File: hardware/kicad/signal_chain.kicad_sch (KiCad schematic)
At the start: 33 parts, among them U901 AD8421ARZ, U902 OPA197IDBV, U903 OPA365AIDBV, U904 ADS8860IDGS

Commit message: feat(hardware)!: draw draft A1 of the schematic around a Pico 2
A Raspberry Pi Pico 2 on two 1x20 sockets replaces the ESP32-S3
development board, the programmable logic device and the buffer
between the two boards (D-39 to D-43 of the specification). The former
interface and range logic sheets become two new ones:

- Controller: the Pico 2, the diodes that join its USB supply and the
  5 V rail of the carrier, resistor arrays in the SPI and acquisition
  lines, a reset button and a console header.
- Side Data: two shift registers that take the range, the status
  signals and the eight logic inputs with every sample.

The DUT connects through a 1x4 pin header and a lever terminal block
in parallel, both GND, VIN, VOUT, GND, and the logic port is a 1x10
header with VCC, GND, D7 to D0: the pin order of the PPK2 (D-44). A
solder jumper selects the supply of the DUT side of the level
translator. A transistor at the driver of the ampere switch holds it
open while VIN is above 5.5 V.

Reference designators are numbered as the annotation tool of KiCad
does by default (D-45). The numbering touches every sheet, so these
changes come in one commit. The symbol and the socket footprint of
the ESP32-S3 board leave the project library; the Pico 2 uses the
symbol and the footprint of the KiCad library.

The electrical rules check reports no errors and no warnings. The
parts stay candidates, and no program for the PIO blocks exists yet.

BREAKING CHANGE: the pins of the controller follow the new pin map of
section 5 of the specification.
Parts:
- renumbered C905 to C57, C908 to C58, C907 to C59, C906 to C60, C901 to C61, C903 to C62, C902 to C63, C909 to C64, C904 to C65, C913 to C66, C912 to C67, C911 to C68, C910 to C69, C914 to C70, C915 to C71, C916 to C72, C917 to C73, C918 to C74, D901 to D10, R902 to R53, R903 to R54, R901 to R55, R904 to R56, R905 to R57, R906 to R58, RN901 to RN3, TP903 to TP22, TP901 to TP23, TP902 to TP24, U902 to U19, U901 to U20, U903 to U21, U904 to U22
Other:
- note added: "U20: G = 1 + 9.9 k / R55 = 19.93. Reference pin at 50 mV: zero current reads about 1300 codes. AMP_RAW can reach 10 V during a range change: R56 and D10 limit the driver input. U21: Sallen-Key, 40 kHz, Q = 0.74. R58 and C70 as the converter input needs. U22: 3-wire mode, DIN high. CONVST is the I2S word clock, SCLK the bit clock. C71 and C72 sit at the REF pin."
- note removed: "U901: G = 1 + 9.9 k / R901 = 19.93. Reference pin at 50 mV: zero current reads about 1300 codes. AMP_RAW can reach 10 V during a range change: R904 and D901 limit the driver input. U903: Sallen-Key, 40 kHz, Q = 0.74. R906 and C914 as the converter input needs. U904: 3-wire mode, DIN high. CONVST is the I2S word clock, SCLK the bit clock. C915 and C916 sit at the REF pin."

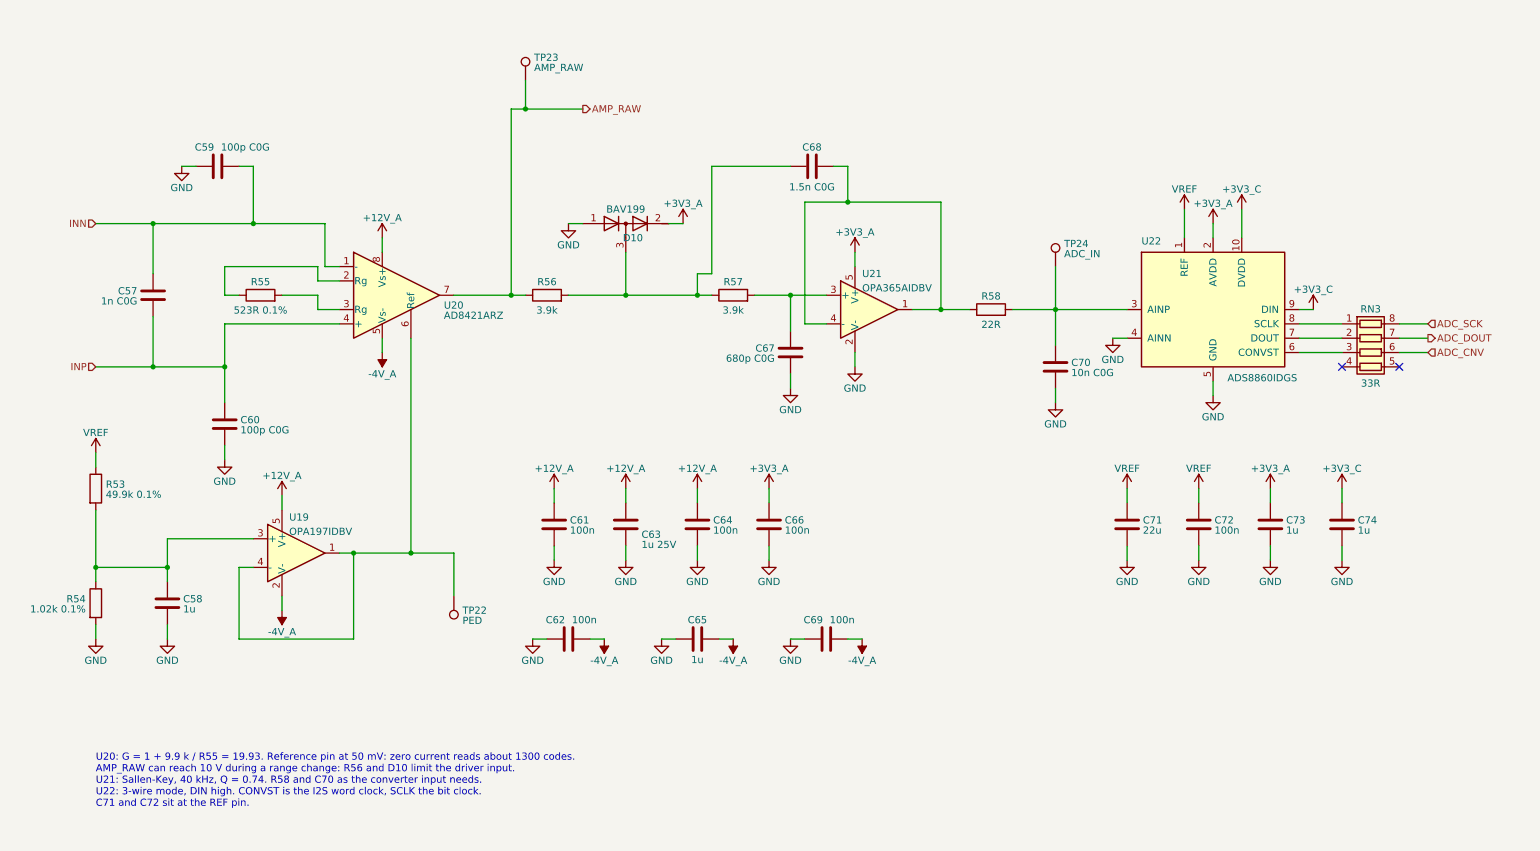
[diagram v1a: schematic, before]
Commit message: feat(hardware): draw draft A2 of the schematic
428 parts on 15 A4 pages, 14 sheets below the root sheet (D-83). Two
sheets are new: Logic Supplies, with the supervisor of the 5 V rail and
the two 3.3 V regulators, and Rail Monitor, with the comparators behind
PWR_GOOD.

The drawings follow the specification of draft A2: a current limiter
on each supply input and a priority multiplexer, a pre-regulator that
tracks the output of the linear regulator, a VIN path that withstands
-20 V to +20 V with its switch open, two diode-connected MOSFETs as
ladder clamp, thin-film and four-terminal shunts, ESD arrays at the CC
pins and at the VCC pin of the logic port. The reference designators
are numbered as KiCad numbers them (D-45), so they are not those of
draft A1.

The project library gains the symbol of the input multiplexer and two
footprints: the lever terminal block with pads of 1.9 mm x 2.3 mm and
the controller module without its antenna keep-out (D-85).

The electrical rules check reports no errors and no warnings. The
parts are candidates, and nothing is built or measured.
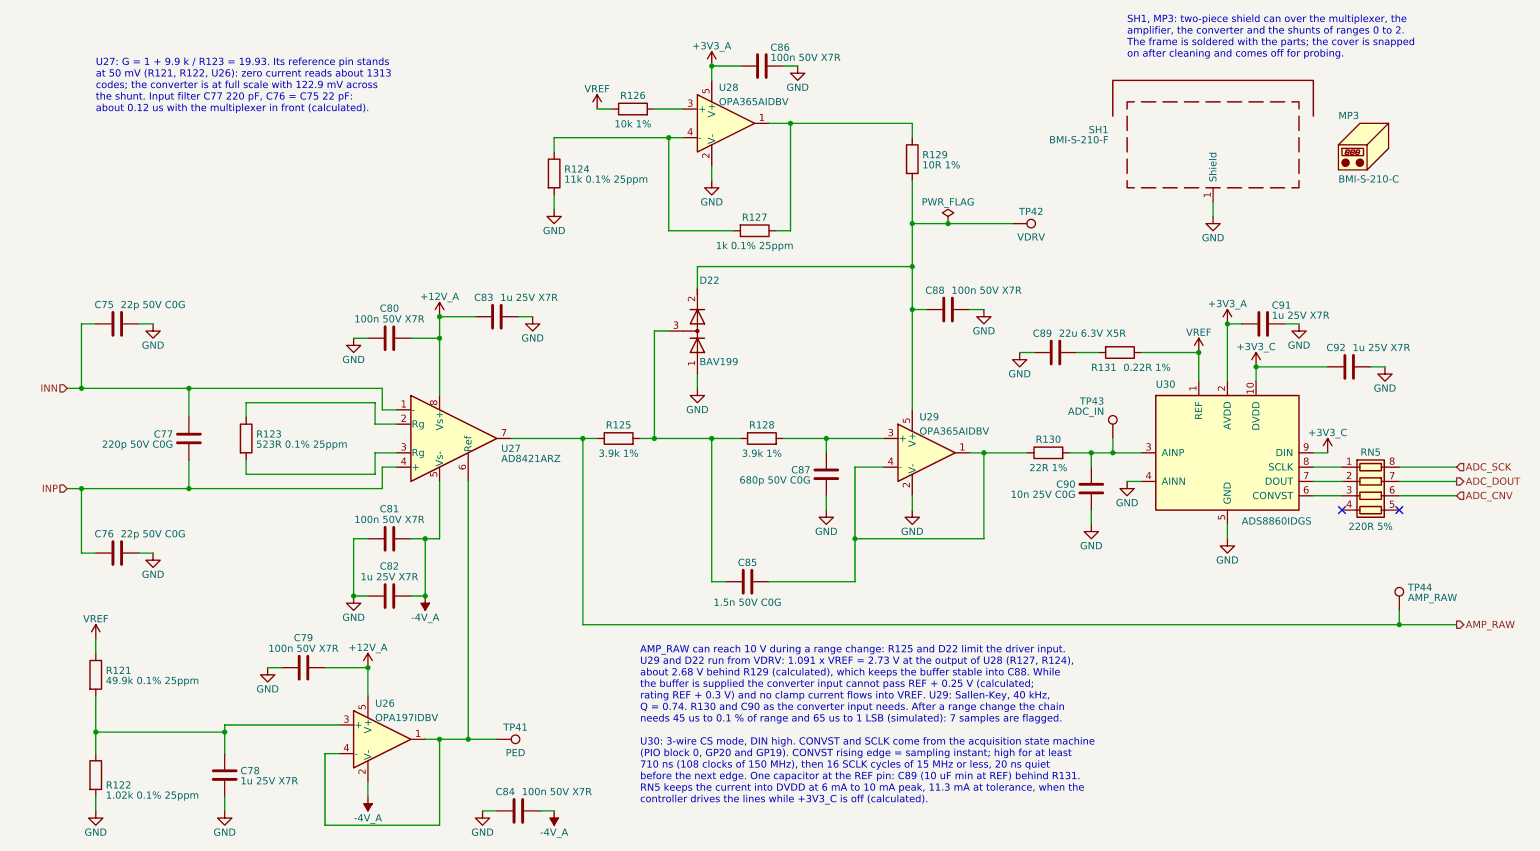
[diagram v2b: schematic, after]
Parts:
- removed C72: 100n, Capacitor_SMD:C_0603_1608Metric, symbol Device:C
- added C86: 100n 50V X7R, Capacitor_SMD:C_0603_1608Metric, symbol Device:C
- added MP3: BMI-S-210-C, symbol Mechanical:Housing
- added R124: 11k 0.1% 25ppm, Resistor_SMD:R_0603_1608Metric, symbol Device:R
- added R126: 10k 1%, Resistor_SMD:R_0603_1608Metric, symbol Device:R
- added R127: 1k 0.1% 25ppm, Resistor_SMD:R_0603_1608Metric, symbol Device:R
- added R129: 10R 1%, Resistor_SMD:R_0603_1608Metric, symbol Device:R
- added R131: 0.22R 1%, Resistor_SMD:R_0603_1608Metric, symbol Device:R
- added SH1: BMI-S-210-F, RF_Shielding:Laird_Technologies_BMI-S-210-F_44.00x30.50mm, symbol Device:RFShield_TwoPieces
- added TP42: VDRV, TestPoint:TestPoint_Pad_D1.5mm, symbol Connector:TestPoint
- added U28: OPA365AIDBV, Package_TO_SOT_SMD:SOT-23-5, symbol Amplifier_Operational:OPA365xxDBV
- C75: renamed from C59; value 100p C0G -> 22p 50V C0G; MPN (none) -> C0603C220J5GACTU; Manufacturer (none) -> KEMET
- C76: renamed from C60; value 100p C0G -> 22p 50V C0G; MPN (none) -> C0603C220J5GACTU; Manufacturer (none) -> KEMET
- C77: renamed from C57; value 1n C0G -> 220p 50V C0G; MPN (none) -> C0603C221J5GACTU; Manufacturer (none) -> KEMET
- C78: renamed from C58; value 1u -> 1u 25V X7R; MPN (none) -> C0603C105K3RACTU; Manufacturer (none) -> KEMET
- C79: renamed from C64; value 100n -> 100n 50V X7R; MPN (none) -> C0603C104K5RACTU; Manufacturer (none) -> KEMET
- C80: renamed from C61; value 100n -> 100n 50V X7R; MPN (none) -> C0603C104K5RACTU; Manufacturer (none) -> KEMET
- C81: renamed from C62; value 100n -> 100n 50V X7R; MPN (none) -> C0603C104K5RACTU; Manufacturer (none) -> KEMET
- C82: renamed from C65; value 1u -> 1u 25V X7R; MPN (none) -> C0603C105K3RACTU; Manufacturer (none) -> KEMET
- C83: renamed from C63; value 1u 25V -> 1u 25V X7R; MPN (none) -> C0603C105K3RACTU; Manufacturer (none) -> KEMET
- C84: renamed from C69; value 100n -> 100n 50V X7R; MPN (none) -> C0603C104K5RACTU; Manufacturer (none) -> KEMET
- C85: renamed from C68; value 1.5n C0G -> 1.5n 50V C0G; MPN (none) -> C0603C152J5GACTU; Manufacturer (none) -> KEMET
- C87: renamed from C67; value 680p C0G -> 680p 50V C0G; MPN (none) -> C0603C681J5GACTU; Manufacturer (none) -> KEMET
- C88: renamed from C66; value 100n -> 100n 50V X7R; MPN (none) -> C0603C104K5RACTU; Manufacturer (none) -> KEMET
- C89: renamed from C71; value 22u -> 22u 6.3V X5R; MPN (none) -> CL21A226KQQNNNE; Manufacturer (none) -> Samsung Electro-Mechanics
- C90: renamed from C70; value 10n C0G -> 10n 25V C0G; MPN (none) -> C0603C103J3GACTU; Manufacturer (none) -> KEMET
- C91: renamed from C73; value 1u -> 1u 25V X7R; MPN (none) -> C0603C105K3RACTU; Manufacturer (none) -> KEMET
- C92: renamed from C74; value 1u -> 1u 25V X7R; MPN (none) -> C0603C105K3RACTU; Manufacturer (none) -> KEMET
- D22: renamed from D10; MPN (none) -> BAV199-7-F; Manufacturer (none) -> Diodes Incorporated
- R121: renamed from R53; value 49.9k 0.1% -> 49.9k 0.1% 25ppm; MPN (none) -> TNPW060349K9BEEA; Manufacturer (none) -> Vishay
- R122: renamed from R54; value 1.02k 0.1% -> 1.02k 0.1% 25ppm; MPN (none) -> TNPW06031K02BEEA; Manufacturer (none) -> Vishay
- R123: renamed from R55; value 523R 0.1% -> 523R 0.1% 25ppm; MPN (none) -> RT0603BRD07523RL; Manufacturer (none) -> Yageo; Note 10 ppm/K, G = 19.93 -> G = 19.93
- R125: renamed from R56; value 3.9k -> 3.9k 1%; MPN (none) -> CRCW06033K90FKEA; Manufacturer (none) -> Vishay
- R128: renamed from R57; value 3.9k -> 3.9k 1%; MPN (none) -> CRCW06033K90FKEA; Manufacturer (none) -> Vishay
- R130: renamed from R58; value 22R -> 22R 1%; MPN (none) -> CRCW060322R0FKEA; Manufacturer (none) -> Vishay
- RN5: renamed from RN3; value 33R -> 220R 5%; MPN (none) -> CAY16-221J4LF; Manufacturer (none) -> Bourns
- TP41: renamed from TP22; now left out of the parts list
- TP43: renamed from TP24; now left out of the parts list
- TP44: renamed from TP23; now left out of the parts list
- U26: renamed from U19; MPN (none) -> OPA197IDBVR; Manufacturer (none) -> Texas Instruments
- U27: renamed from U20; MPN (none) -> AD8421ARZ; Manufacturer (none) -> Analog Devices
- U29: renamed from U21; MPN (none) -> OPA365AIDBVR; Manufacturer (none) -> Texas Instruments
- U30: renamed from U22; MPN (none) -> ADS8860IDGS; Manufacturer (none) -> Texas Instruments
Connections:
- net +3V3_A: now also C86.1, U28.5 (V+); no longer C88.1, D22.2 (K), U29.5 (V+)
- net GND: now also C86.2, R124.2, SH1.1 (Shield), U28.2 (V-)
- net VREF: now also R126.1, R131.1; no longer C89.1
- new net: C88.1, D22.2 (K), R129.2, TP42.1, U29.5 (V+)
- new net: C89.1, R131.2
- new net: R127.1, R129.1, U28.1
- new net: R124.1, R127.2, U28.4 (-)
- new net: R126.2, U28.3 (+)
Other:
- note added: "AMP_RAW can reach 10 V during a range change: R125 and D22 limit the driver input. U29 and D22 run from VDRV: 1.091 x VREF = 2.73 V at the output of U28 (R127, R124), about 2.68 V behind R129 (calculated), which keeps the buffer stable into C88. While the buffer is supplied the converter input cannot pass REF + 0.25 V (calculated; rating REF + 0.3 V) and no clamp current flows into VREF. U29: Sal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"
- note added: "SH1, MP3: two-piece shield can over the multiplexer, the amplifier, the converter and the shunts of ranges 0 to 2. The frame is soldered with the parts; the cover is snapped on after cleaning and comes off for probing."
- note added: "U27: G = 1 + 9.9 k / R123 = 19.93. Its reference pin stands at 50 mV (R121, R122, U26): zero current reads about 1313 codes; the converter is at full scale with 122.9 mV across the shunt. Input filter C77 220 pF, C76 = C75 22 pF: about 0.12 us with the multiplexer in front (calculated)."
- note removed: "U20: G = 1 + 9.9 k / R55 = 19.93. Reference pin at 50 mV: zero current reads about 1300 codes. AMP_RAW can reach 10 V during a range change: R56 and D10 limit the driver input. U21: Sallen-Key, 40 kHz, Q = 0.74. R58 and C70 as the converter input needs. U22: 3-wire mode, DIN high. CONVST is the I2S word clock, SCLK the bit clock. C71 and C72 sit at the REF pin."
- moved on the sheet: C75, C76, C77, C78, C79, C80, C81, C82, C83, C84, C85, C87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
